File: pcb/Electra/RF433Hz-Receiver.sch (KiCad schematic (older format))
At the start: 4 parts, among them J801 Conn_01x04_Female, Q801 BSS138

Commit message: PCB completed (added silkscreen more)
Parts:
- J801: value Conn_01x04_Female -> RF433
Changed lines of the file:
@@
 AR Path="/605DAAEC/605DECF5" Ref="J801"  Part="1"
 F 0 "J801" H 7528 3776 50  0000 L CNN
-F 1 "Conn_01x04_Female" H 7528 3685 50  0000 L CNN
+F 1 "RF433" H 7528 3685 50  0000 L CNN
 F 2 "Connector_PinHeader_2.54mm:PinHeader_1x04_P2.54mm_Vertical" H 7500 3800 50  0001 C CNN
 F 3 "-" H 7500 3800 50  0001 C CNN

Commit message: Rev 2 completed, todo check all and remove not needed filed
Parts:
- removed Q801: BSS138, Package_TO_SOT_SMD:SOT-23, symbol Transistor_FET:BSS138
- removed R801, R802: 10K, Resistor_SMD:R_0603_1608Metric_Pad0.98x0.95mm_HandSolder, symbol Device:R
- added R701: 1K, Resistor_SMD:R_0603_1608Metric_Pad0.98x0.95mm_HandSolder, symbol Device:R
- added R702: 2K, Resistor_SMD:R_0603_1608Metric_Pad0.98x0.95mm_HandSolder, symbol Device:R
- J701: renamed from J801; Description - -> (none); LCSC Part # - -> (none); Manufacturer - -> (none); Maximum Value - -> (none); Mfr.Part # - -> (none)
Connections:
- net GND: now also R702.2
- net output: now also R701.2, R702.1
- net at J701.2 (Pin_2): now also R701.1
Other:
- moved on the sheet: J701
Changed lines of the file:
@@
 $Descr A4 11693 8268
 encoding utf-8
-Sheet 8 8
-Title ""
-Date ""
-Rev ""
-Comp ""
-Comment1 ""
-Comment2 ""
+Sheet 7 8
+Title "Electra Project"
+Date "2021-04-01"
+Rev "2.0"
+Comp "Grehasopt"
+Comment1 "https://github.com/Grehasopt/Electra"
+Comment2 "Remote Relay Switches"
 Comment3 ""
 Comment4 ""
 $EndDescr
+NoConn ~ 5105 3085
+Text Notes 5180 2545 2    50   ~ 0
+External RF433Mhz module header connection
 Wire Wire Line
-	5600 3400 5600 3450
-Connection ~ 5600 3400
+	5255 2885 5255 2835
 Wire Wire Line
-	6000 3400 6000 3500
+	5105 2885 5255 2885
 Wire Wire Line
-	5600 3400 6000 3400
+	5255 3185 5255 3235
 Wire Wire Line
-	5600 3800 5600 3750
-Wire Wire Line
-	5800 3800 5600 3800
-Wire Wire Line
-	6350 3800 6200 3800
-Wire Wire Line
-	6350 3750 6350 3800
-Wire Wire Line
-	6350 3350 6350 3450
+	5105 3185 5255 3185
 $Comp
 L power:+5V #PWR?
-U 1 1 605DED28
-P 6350 3350
-AR Path="/605DED28" Ref="#PWR?"  Part="1"
-AR Path="/605DAAEC/605DED28" Ref="#PWR0802"  Part="1"
-F 0 "#PWR0802" H 6350 3200 50  0001 C CNN
-F 1 "+5V" H 6365 3523 50  0000 C CNN
-F 2 "" H 6350 3350 50  0001 C CNN
-F 3 "" H 6350 3350 50  0001 C CNN
-	1    6350 3350
-	1    0    0    -1
+U 1 1 605DED01
+P 5255 2835
+AR Path="/605DED01" Ref="#PWR?"  Part="1"
+AR Path="/605DAAEC/605DED01" Ref="#PWR0701"  Part="1"
+F 0 "#PWR0701" H 5255 2685 50  0001 C CNN
+F 1 "+5V" H 5270 3008 50  0000 C CNN
+F 2 "" H 5255 2835 50  0001 C CNN
+F 3 "" H 5255 2835 50  0001 C CNN
+	1    5255 2835
+	-1   0    0    -1
 $EndComp
-Wire Wire Line
-	5600 3350 5600 3400
 $Comp
-L power:+3V3 #PWR?
-U 1 1 605DED21
-P 5600 3350
-AR Path="/605DED21" Ref="#PWR?"  Part="1"
-AR Path="/605DAAEC/605DED21" Ref="#PWR0801"  Part="1"
-F 0 "#PWR0801" H 5600 3200 50  0001 C CNN
-F 1 "+3V3" V 5615 3478 50  0000 L CNN
-F 2 "" H 5600 3350 50  0001 C CNN
-F 3 "" H 5600 3350 50  0001 C CNN
-	1    5600 3350
+L power:GND #PWR?
+U 1 1 605DECFB
+P 5255 3235
+AR Path="/605DECFB" Ref="#PWR?"  Part="1"
+AR Path="/605DAAEC/605DECFB" Ref="#PWR0702"  Part="1"
+F 0 "#PWR0702" H 5255 2985 50  0001 C CNN
+F 1 "GND" H 5260 3062 50  0000 C CNN
+F 2 "" H 5255 3235 50  0001 C CNN
+F 3 "" H 5255 3235 50  0001 C CNN
+	1    5255 3235
+	-1   0    0    -1
+$EndComp
+$Comp
+L Connector:Conn_01x04_Female J?
+U 1 1 605DECF5
+P 4905 2985
+AR Path="/605DECF5" Ref="J?"  Part="1"
+AR Path="/605DAAEC/605DECF5" Ref="J701"  Part="1"
+F 0 "J701" H 4933 2961 50  0000 L CNN
+F 1 "RF433" H 4933 2870 50  0000 L CNN
+F 2 "Connector_PinHeader_2.54mm:PinHeader_1x04_P2.54mm_Vertical" H 4905 2985 50  0001 C CNN
+F 3 "~" H 4905 2985 50  0001 C CNN
+F 4 "2.54mm 1x4" H 4905 2985 50  0001 C CNN "Package Reference"
+	1    4905 2985
+	-1   0    0    -1
+$EndComp
+Text HLabel 6610 3565 2    50   Output ~ 0
+output
+$Comp
+L Device:R R701
+U 1 1 60652FFB
+P 6050 3270
+F 0 "R701" H 6120 3316 50  0000 L CNN
+F 1 "1K" V 6050 3190 50  0000 L CNN
+F 2 "Resistor_SMD:R_0603_1608Metric_Pad0.98x0.95mm_HandSolder" V 5980 3270 50  0001 C CNN
+F 3 "~" H 6050 3270 50  0001 C CNN
+F 4 "0603" H 6050 3270 50  0001 C CNN "Package Reference"
+F 5 "0.1W" H 6050 3270 50  0001 C CNN "Maximum Value"
+F 6 "C21190" H 6050 3270 50  0001 C CNN "LCSC"
+	1    6050 3270
 	1    0    0    -1
 $EndComp
 $Comp
-L Device:R R?
-U 1 1 605DED1B
-P 6350 3600
-AR Path="/605DED1B" Ref="R?"  Part="1"
-AR Path="/605DAAEC/605DED1B" Ref="R802"  Part="1"
-F 0 "R802" H 6420 3646 50  0000 L CNN
-F 1 "10K" V 6350 3500 50  0000 L CNN
-F 2 "Resistor_SMD:R_0603_1608Metric_Pad0.98x0.95mm_HandSolder" V 6280 3600 50  0001 C CNN
-F 3 "https://datasheet.lcsc.com/szlcsc/1809140220_UNI-ROYAL-Uniroyal-Elec-0603WAJ0103T5E_C15401.pdf" H 6350 3600 50  0001 C CNN
-F 4 "10kΩ ±5% 0.1W ±100ppm/℃ 0603 Chip Resistor - Surface Mount RoHS" H 6350 3600 50  0001 C CNN "Description"
-F 5 "C15401" H 6350 3600 50  0001 C CNN "LCSC Part #"
-F 6 "UNI-ROYAL(Uniroyal Elec)" H 6350 3600 50  0001 C CNN "Manufacturer"
-F 7 "0.1W" H 6350 3600 50  0001 C CNN "Maximum Value"
-F 8 "0603WAJ0103T5E" H 6350 3600 50  0001 C CNN "Mfr.Part #"
-F 9 "0603" H 6350 3600 50  0001 C CNN "Package Reference"
-	1    6350 3600
-	1    0    0    -1
-$EndComp
-$Comp
-L Device:R R?
-U 1 1 605DED15
-P 5600 3600
-AR Path="/605DED15" Ref="R?"  Part="1"
-AR Path="/605DAAEC/605DED15" Ref="R801"  Part="1"
-F 0 "R801" H 5670 3646 50  0000 L CNN
-F 1 "10K" V 5600 3500 50  0000 L CNN
-F 2 "Resistor_SMD:R_0603_1608Metric_Pad0.98x0.95mm_HandSolder" V 5530 3600 50  0001 C CNN
-F 3 "https://datasheet.lcsc.com/szlcsc/1809140220_UNI-ROYAL-Uniroyal-Elec-0603WAJ0103T5E_C15401.pdf" H 5600 3600 50  0001 C CNN
-F 4 "10kΩ ±5% 0.1W ±100ppm/℃ 0603 Chip Resistor - Surface Mount RoHS" H 5600 3600 50  0001 C CNN "Description"
-F 5 "C15401" H 5600 3600 50  0001 C CNN "LCSC Part #"
-F 6 "UNI-ROYAL(Uniroyal Elec)" H 5600 3600 50  0001 C CNN "Manufacturer"
-F 7 "0.1W" H 5600 3600 50  0001 C CNN "Maximum Value"
-F 8 "0603WAJ0103T5E" H 5600 3600 50  0001 C CNN "Mfr.Part #"
-F 9 "0603" H 5600 3600 50  0001 C CNN "Package Reference"
-	1    5600 3600
-	1    0    0    -1
-$EndComp
-$Comp
-L Transistor_FET:BSS138 Q?
-U 1 1 605DED0F
-P 6000 3700
-AR Path="/605DED0F" Ref="Q?"  Part="1"
-AR Path="/605DAAEC/605DED0F" Ref="Q801"  Part="1"
-F 0 "Q801" V 6249 3700 50  0000 C CNN
-F 1 "BSS138" V 6340 3700 50  0000 C CNN
-F 2 "Package_TO_SOT_SMD:SOT-23" H 6200 3625 50  0001 L CIN
-F 3 "https://datasheet.lcsc.com/szlcsc/1912111437_Slkor-SLKORMICRO-Elec-BSS138_C426569.pdf" H 6000 3700 50  0001 L CNN
-F 4 "N-Channel 50V 220mA 1.6V @ 1mA 3.5Ω @ 220mA,10V 225mW SOT-23 MOSFET RoHS" H 6000 3700 50  0001 C CNN "Description"
-F 5 "C426569" H 6000 3700 50  0001 C CNN "LCSC Part #"
-F 6 "Slkor(SLKORMICRO Elec.)" H 6000 3700 50  0001 C CNN "Manufacturer"
-F 7 "Vdss= 50V , Id =  220mA " H 6000 3700 50  0001 C CNN "Maximum Value"
-F 8 "BSS138" H 6000 3700 50  0001 C CNN "Mfr.Part #"
-F 9 "SOT-23" H 6000 3700 50  0001 C CNN "Package Reference"
-	1    6000 3700
-	0    1    1    0
-$EndComp
-NoConn ~ 7300 3900
-Text Notes 7350 3550 0    50   ~ 0
-External RF433Mhz module header connection
-Wire Wire Line
-	7150 3700 7150 3650
-Wire Wire Line
-	7300 3700 7150 3700
-Wire Wire Line
-	7150 4000 7150 4050
-Wire Wire Line
-	7300 4000 7150 4000
-$Comp
-L power:+5V #PWR?
-U 1 1 605DED01
-P 7150 3650
-AR Path="/605DED01" Ref="#PWR?"  Part="1"
-AR Path="/605DAAEC/605DED01" Ref="#PWR0803"  Part="1"
-F 0 "#PWR0803" H 7150 3500 50  0001 C CNN
-F 1 "+5V" H 7165 3823 50  0000 C CNN
-F 2 "" H 7150 3650 50  0001 C CNN
-F 3 "" H 7150 3650 50  0001 C CNN
-	1    7150 3650
+L Device:R R702
+U 1 1 60653447
+P 6050 3880
+F 0 "R702" H 6120 3926 50  0000 L CNN
+F 1 "2K" V 6050 3810 50  0000 L CNN
+F 2 "Resistor_SMD:R_0603_1608Metric_Pad0.98x0.95mm_HandSolder" V 5980 3880 50  0001 C CNN
+F 3 "~" H 6050 3880 50  0001 C CNN
+F 4 "0603" H 6050 3880 50  0001 C CNN "Package Reference"
+F 5 "0.1W" H 6050 3880 50  0001 C CNN "Maximum Value"
+F 6 "C22975" H 6050 3880 50  0001 C CNN "LCSC"
+	1    6050 3880
 	1    0    0    -1
 $EndComp
 $Comp
 L power:GND #PWR?
-U 1 1 605DECFB
-P 7150 4050
-AR Path="/605DECFB" Ref="#PWR?"  Part="1"
-AR Path="/605DAAEC/605DECFB" Ref="#PWR0804"  Part="1"
-F 0 "#PWR0804" H 7150 3800 50  0001 C CNN
-F 1 "GND" H 7155 3877 50  0000 C CNN
-F 2 "" H 7150 4050 50  0001 C CNN
-F 3 "" H 7150 4050 50  0001 C CNN
-	1    7150 4050
-	1    0    0    -1
+U 1 1 60653B33
+P 6050 4230
+AR Path="/60653B33" Ref="#PWR?"  Part="1"
+AR Path="/605DAAEC/60653B33" Ref="#PWR0703"  Part="1"
+F 0 "#PWR0703" H 6050 3980 50  0001 C CNN
+F 1 "GND" H 6055 4057 50  0000 C CNN
+F 2 "" H 6050 4230 50  0001 C CNN
+F 3 "" H 6050 4230 50  0001 C CNN
+	1    6050 4230
+	-1   0    0    -1
 $EndComp
-$Comp
-L Connector:Conn_01x04_Female J?
-U 1 1 605DECF5
-P 7500 3800
-AR Path="/605DECF5" Ref="J?"  Part="1"
-AR Path="/605DAAEC/605DECF5" Ref="J801"  Part="1"
-F 0 "J801" H 7528 3776 50  0000 L CNN
-F 1 "RF433" H 7528 3685 50  0000 L CNN
-F 2 "Connector_PinHeader_2.54mm:PinHeader_1x04_P2.54mm_Vertical" H 7500 3800 50  0001 C CNN
-F 3 "-" H 7500 3800 50  0001 C CNN
-F 4 "-" H 7500 3800 50  0001 C CNN "Mfr.Part #"
-F 5 "2.54mm 1x4" H 7500 3800 50  0001 C CNN "Package Reference"
-F 6 "-" H 7500 3800 50  0001 C CNN "Description"
-F 7 "-" H 7500 3800 50  0001 C CNN "LCSC Part #"
-F 8 "-" H 7500 3800 50  0001 C CNN "Manufacturer"
-F 9 "-" H 7500 3800 50  0001 C CNN "Maximum Value"
-	1    7500 3800
-	1    0    0    -1
-$EndComp
-Connection ~ 6350 3800
 Wire Wire Line
-	6350 3800 7300 3800
-Text HLabel 4800 3800 0    50   Output ~ 0
-output
+	6050 4030 6050 4230
 Wire Wire Line
-	5600 3800 4800 3800
-Connection ~ 5600 3800
+	6050 3730 6050 3565
+Wire Wire Line
+	5105 2985 6050 2985
+Wire Wire Line
+	6050 2985 6050 3120
+Wire Wire Line
+	6610 3565 6050 3565
+Connection ~ 6050 3565
+Wire Wire Line
+	6050 3565 6050 3420
 $EndSCHEMATC

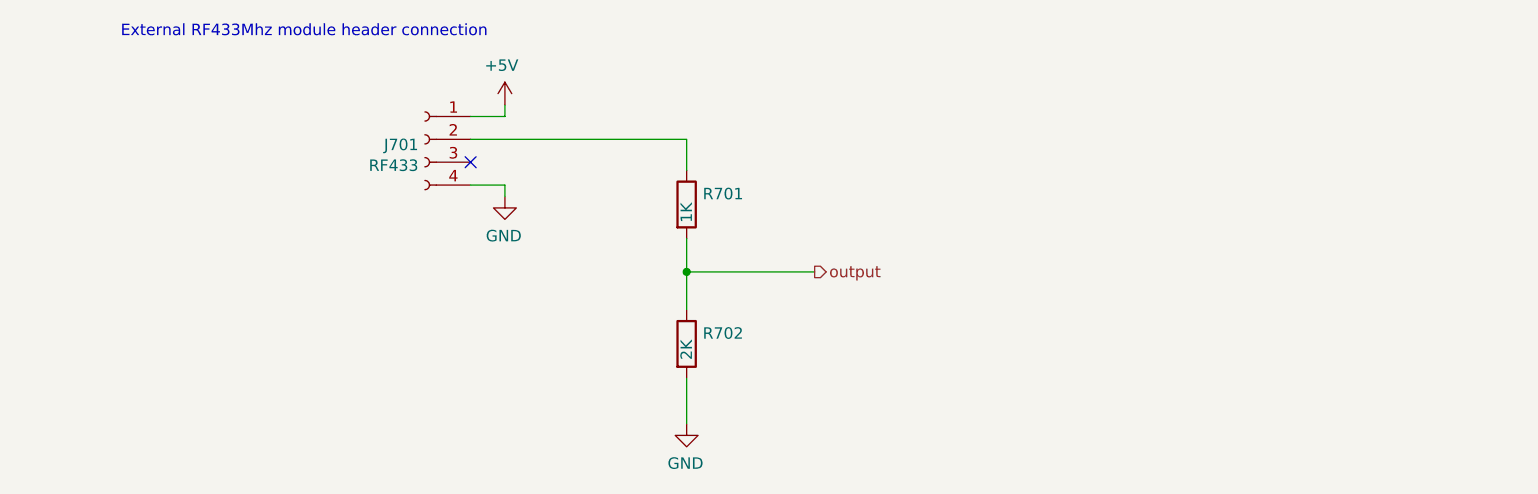
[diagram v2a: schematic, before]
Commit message: Minor fixes on schematic and pcb fix bjt netlist + ac main voltage to both sides (Rev 2.1)
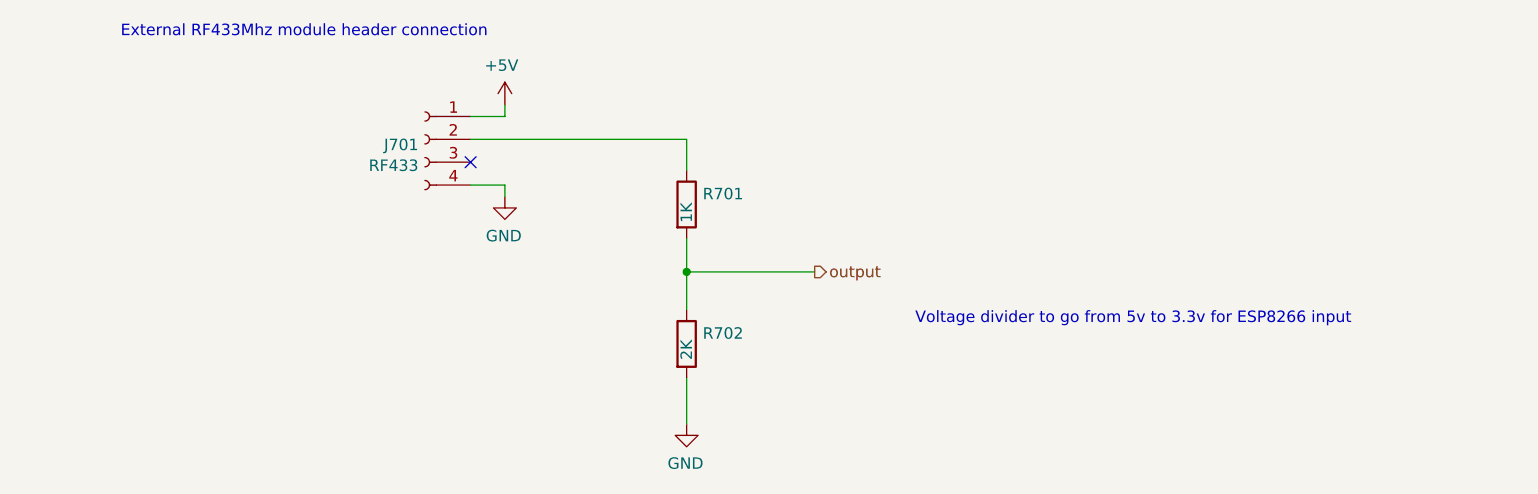
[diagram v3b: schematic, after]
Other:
- note added: "Voltage divider to go from 5v to 3.3v for ESP8266 input"
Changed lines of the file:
@@
 Sheet 7 8
 Title "Electra Project"
-Date "2021-04-01"
-Rev "2.0"
+Date "2021-05-04"
+Rev "2.1"
 Comp "Grehasopt"
 Comment1 "https://github.com/Grehasopt/Electra"
@@
 Wire Wire Line
 	6050 3565 6050 3420
+Text Notes 7050 3800 0    50   ~ 0
+Voltage divider to go from 5v to 3.3v for ESP8266 input
 $EndSCHEMATC
